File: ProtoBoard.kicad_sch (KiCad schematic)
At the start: 53 parts, among them IC1 L9110S, IC2 L9110S, IC3 L9110S, J1 Conn_01x02_Female, J11 Conn_01x10_Female, J2 Conn_01x08_Female, J3 I2C_STANDARDQWIIC, J4 Conn_01x10_Female, J5 Conn_01x05_Female, J6 Conn_01x05_Female, J7 Conn_01x10_Female, J8 Conn_01x05_Female, J9 Conn_01x10_Female, U1 ESP32-WROOM-32D, U10 SY6280AAC, U2 CD74HC4067SM, U3 LM1084-5.0, U4 CD74HC4067SM, U6 LM1084-3.3, U7 SY6280AAC, U8 SY6280AAC, U9 SY6280AAC

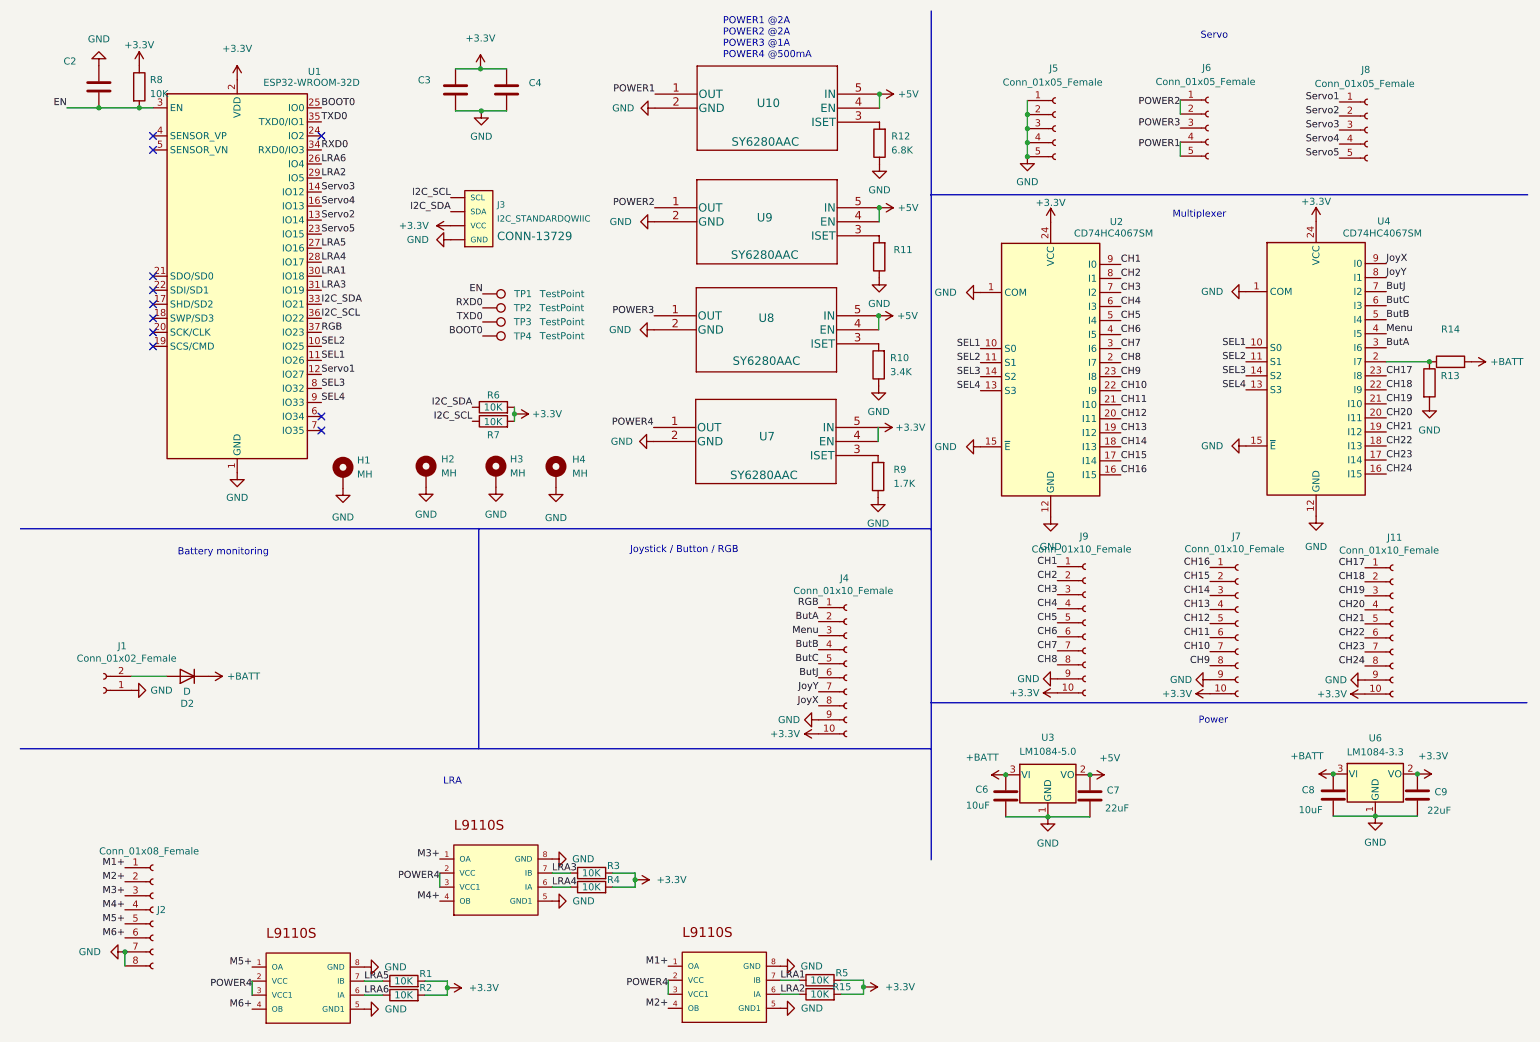
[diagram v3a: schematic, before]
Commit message: Remove diode
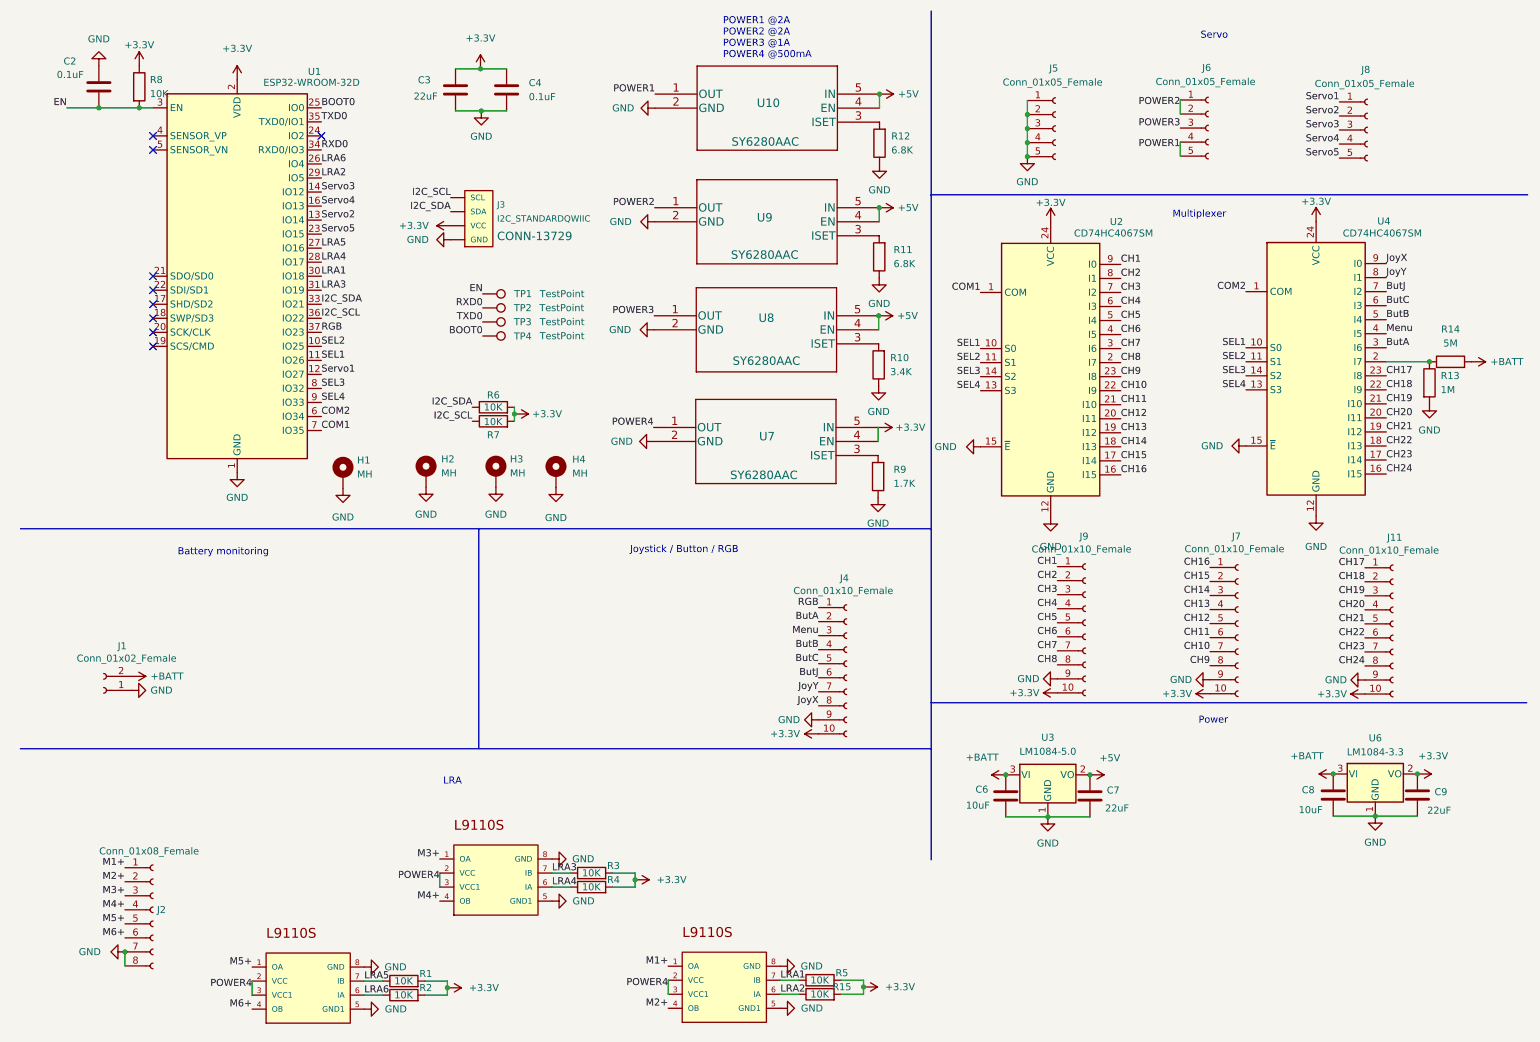
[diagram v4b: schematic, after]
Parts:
- removed D2: D, Diode_SMD:D_0402_1005Metric, symbol Device:D
- C2, C4: value (none) -> 0.1uF
- C3: value (none) -> 22uF
- R11: value (none) -> 6.8K
- R13: value (none) -> 1M
- R14: value (none) -> 5M
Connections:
- net +BATT: now also J1.2 (Pin_2)
- net GND: no longer U2.1 (COM), U4.1 (COM)
- net COM2: now reaches U1.6 (IO34)
- net COM2: now also U4.1 (COM)
- net COM1: now reaches U1.7 (IO35)
- net COM1: now also U2.1 (COM)
- no-connect marks 11 -> 9
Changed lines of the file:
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@@
   (no_connect (at 36.1188 34.8488))
   (no_connect (at 36.1188 37.3888))
-  (no_connect (at 66.5988 88.1888))
-  (no_connect (at 66.5988 85.6488))
   (polyline (pts (xy 95.0976 105.918) (xy 95.0976 145.796))
     (stroke (width 0) (type default) (color 0 0 0 0))
@@
     (stroke (width 0) (type default) (color 0 0 0 0))
   )
-  (wire (pts (xy 32.258 132.6896) (xy 38.5064 132.6896))
-    (stroke (width 0) (type default) (color 0 0 0 0))
-  )
   (wire (pts (xy 194.4116 28.448) (xy 194.4116 30.988))
     (stroke (width 0) (type default) (color 0 0 0 0))
@@
     (effects (font (size 1.27 1.27)) (justify right bottom))
   )
+  (label "COM2" (at 233.9848 63.0428 180)
+    (effects (font (size 1.27 1.27)) (justify right bottom))
+  )
   (label "ButC" (at 259.3848 65.5828 0)
     (effects (font (size 1.27 1.27)) (justify left bottom))
@@
     (effects (font (size 1.27 1.27)) (justify left bottom))
   )
+  (label "COM2" (at 66.5988 85.6488 0)
+    (effects (font (size 1.27 1.27)) (justify left bottom))
+  )
   (label "RXD0" (at 66.5988 37.3888 0)
     (effects (font (size 1.27 1.27)) (justify left bottom))
@@
     (effects (font (size 1.27 1.27)) (justify left bottom))
   )
+  (label "COM1" (at 185.928 63.1952 180)
+    (effects (font (size 1.27 1.27)) (justify right bottom))
+  )
   (label "M2+" (at 31.0388 169.8752 180)
     (effects (font (size 1.27 1.27)) (justify right bottom))
@@
   (label "CH1" (at 199.8472 112.8268 180)
     (effects (font (size 1.27 1.27)) (justify right bottom))
+  )
+  (label "COM1" (at 66.5988 88.1888 0)
+    (effects (font (size 1.27 1.27)) (justify left bottom))
   )
   (label "LRA1" (at 66.5988 60.2488 0)
@@
     )
     (property "Datasheet" "" (id 3) (at 70.5104 98.6536 0)
-      (effects (font (size 1.27 1.27)) hide)
-    )
-    (pin "1")
-  )
-  (symbol (lib_id "power:GND") (at 185.928 63.1952 270) (unit 1)
-    (in_bom yes) (on_board yes) (fields_autoplaced)
-    (property "Reference" "#PWR0145" (id 0) (at 179.578 63.1952 0)
-      (effects (font (size 1.27 1.27)) hide)
-    )
-    (property "Value" "GND" (id 1) (at 181.61 63.1951 90)
-      (effects (font (size 1.27 1.27)) (justify right))
-    )
-    (property "Footprint" "" (id 2) (at 185.928 63.1952 0)
-      (effects (font (size 1.27 1.27)) hide)
-    )
-    (property "Datasheet" "" (id 3) (at 185.928 63.1952 0)
       (effects (font (size 1.27 1.27)) hide)
     )
@@
       (effects (font (size 1.27 1.27)) (justify left))
     )
-    (property "Value" "" (id 1) (at 269.24 80.8227 0)
+    (property "Value" "1M" (id 1) (at 269.24 80.8227 0)
       (effects (font (size 1.27 1.27)) (justify left))
     )
@@
       (effects (font (size 1.27 1.27)) (justify left))
     )
-    (property "Value" "" (id 1) (at 104.14 27.7875 0)
+    (property "Value" "0.1uF" (id 1) (at 104.14 27.7875 0)
       (effects (font (size 1.27 1.27)) (justify left))
     )
@@
     (in_bom yes) (on_board yes) (fields_autoplaced)
     (property "Reference" "R14" (id 0) (at 271.018 69.85 90))
-    (property "Value" "" (id 1) (at 271.018 72.39 90))
+    (property "Value" "5M" (id 1) (at 271.018 72.39 90))
     (property "Footprint" "Resistor_SMD:R_0402_1005Metric" (id 2) (at 271.018 77.5208 90)
       (effects (font (size 1.27 1.27)) hide)
@@
       (effects (font (size 1.27 1.27)) (justify left))
     )
-    (property "Value" "" (id 1) (at 83.312 27.686 0)
+    (property "Value" "22uF" (id 1) (at 83.312 27.686 0)
       (effects (font (size 1.27 1.27)) (justify left))
     )
@@
       (effects (font (size 1.27 1.27)) (justify left))
     )
-    (property "Value" "" (id 1) (at 18.6944 23.7744 0)
+    (property "Value" "0.1uF" (id 1) (at 18.6944 23.7744 0)
       (effects (font (size 1.27 1.27)) (justify left))
     )
@@
     (pin "1")
   )
-  (symbol (lib_id "power:GND") (at 233.9848 63.0428 270) (unit 1)
-    (in_bom yes) (on_board yes) (fields_autoplaced)
-    (property "Reference" "#PWR0144" (id 0) (at 227.6348 63.0428 0)
-      (effects (font (size 1.27 1.27)) hide)
-    )
-    (property "Value" "GND" (id 1) (at 229.87 63.0427 90)
-      (effects (font (size 1.27 1.27)) (justify right))
-    )
-    (property "Footprint" "" (id 2) (at 233.9848 63.0428 0)
-      (effects (font (size 1.27 1.27)) hide)
-    )
-    (property "Datasheet" "" (id 3) (at 233.9848 63.0428 0)
-      (effects (font (size 1.27 1.27)) hide)
-    )
-    (pin "1")
-  )
   (symbol (lib_id "L9110S:L9110S") (at 139.5476 190.246 0) (unit 1)
     (in_bom yes) (on_board yes) (fields_autoplaced)
@@
     (pin "1")
   )
-  (symbol (lib_id "power:+BATT") (at 46.1264 132.6896 270) (unit 1)
-    (in_bom yes) (on_board yes) (fields_autoplaced)
-    (property "Reference" "#PWR0122" (id 0) (at 42.3164 132.6896 0)
-      (effects (font (size 1.27 1.27)) hide)
-    )
-    (property "Value" "+BATT" (id 1) (at 49.53 132.6897 90)
-      (effects (font (size 1.27 1.27)) (justify left))
-    )
-    (property "Footprint" "" (id 2) (at 46.1264 132.6896 0)
-      (effects (font (size 1.27 1.27)) hide)
-    )
-    (property "Datasheet" "" (id 3) (at 46.1264 132.6896 0)
+  (symbol (lib_id "power:+BATT") (at 32.258 132.6896 270) (unit 1)
+    (in_bom yes) (on_board yes) (fields_autoplaced)
+    (property "Reference" "#PWR0122" (id 0) (at 28.448 132.6896 0)
+      (effects (font (size 1.27 1.27)) hide)
+    )
+    (property "Value" "+BATT" (id 1) (at 35.6616 132.6897 90)
+      (effects (font (size 1.27 1.27)) (justify left))
+    )
+    (property "Footprint" "" (id 2) (at 32.258 132.6896 0)
+      (effects (font (size 1.27 1.27)) hide)
+    )
+    (property "Datasheet" "" (id 3) (at 32.258 132.6896 0)
       (effects (font (size 1.27 1.27)) hide)
     )
@@
       (effects (font (size 1.27 1.27)) (justify right))
     )
-    (property "Value" "" (id 1) (at 170.18 58.0135 0)
+    (property "Value" "6.8K" (id 1) (at 170.18 58.0135 0)
       (effects (font (size 1.27 1.27)) (justify right))
     )
@@
     (pin "5")
   )
-  (symbol (lib_id "Device:D") (at 42.3164 132.6896 180) (unit 1)
-    (in_bom yes) (on_board yes)
-    (property "Reference" "D2" (id 0) (at 42.3164 137.6172 0))
-    (property "Value" "D" (id 1) (at 42.2656 135.4328 0))
-    (property "Footprint" "Diode_SMD:D_0402_1005Metric" (id 2) (at 42.3164 132.6896 0)
-      (effects (font (size 1.27 1.27)) hide)
-    )
-    (property "Datasheet" "~" (id 3) (at 42.3164 132.6896 0)
-      (effects (font (size 1.27 1.27)) hide)
-    )
-    (pin "1")
-    (pin "2")
-  )
   (symbol (lib_id "Device:R") (at 167.386 96.52 180) (unit 1)
     (in_bom yes) (on_board yes) (fields_autoplaced)
@@
       (reference "#PWR0143") (unit 1) (value "+3.3V") (footprint "")
     )
-    (path "/cd1c2089-35e2-409a-b9f0-0d4c29275ba5"
-      (reference "#PWR0144") (unit 1) (value "GND") (footprint "")
-    )
-    (path "/0dcd0c40-b80f-4055-8c34-88a977438569"
-      (reference "#PWR0145") (unit 1) (value "GND") (footprint "")
-    )
     (path "/0c128885-02be-43f6-b48b-833e50cb9796"
       (reference "#PWR0146") (unit 1) (value "GND") (footprint "")
@@
       (reference "C9") (unit 1) (value "22uF") (footprint "Capacitor_SMD:C_0402_1005Metric")
     )
-    (path "/ec78662d-faa2-4d43-915d-1d9767fd5f16"
-      (reference "D2") (unit 1) (value "D") (footprint "Diode_SMD:D_0402_1005Metric")
-    )
     (path "/73376ead-5128-45e3-9d0b-0f909b2f0f4d"
